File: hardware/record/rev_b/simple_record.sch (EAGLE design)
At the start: 24 parts, among them J1 SQUALL_HEADER, J2 PJ-102AH, J3 SCREW-TERMINAL_2_0.100, J4 SCREW-TERMINAL_2_0.100, Q1 MOSFET-NCHANNELSMD

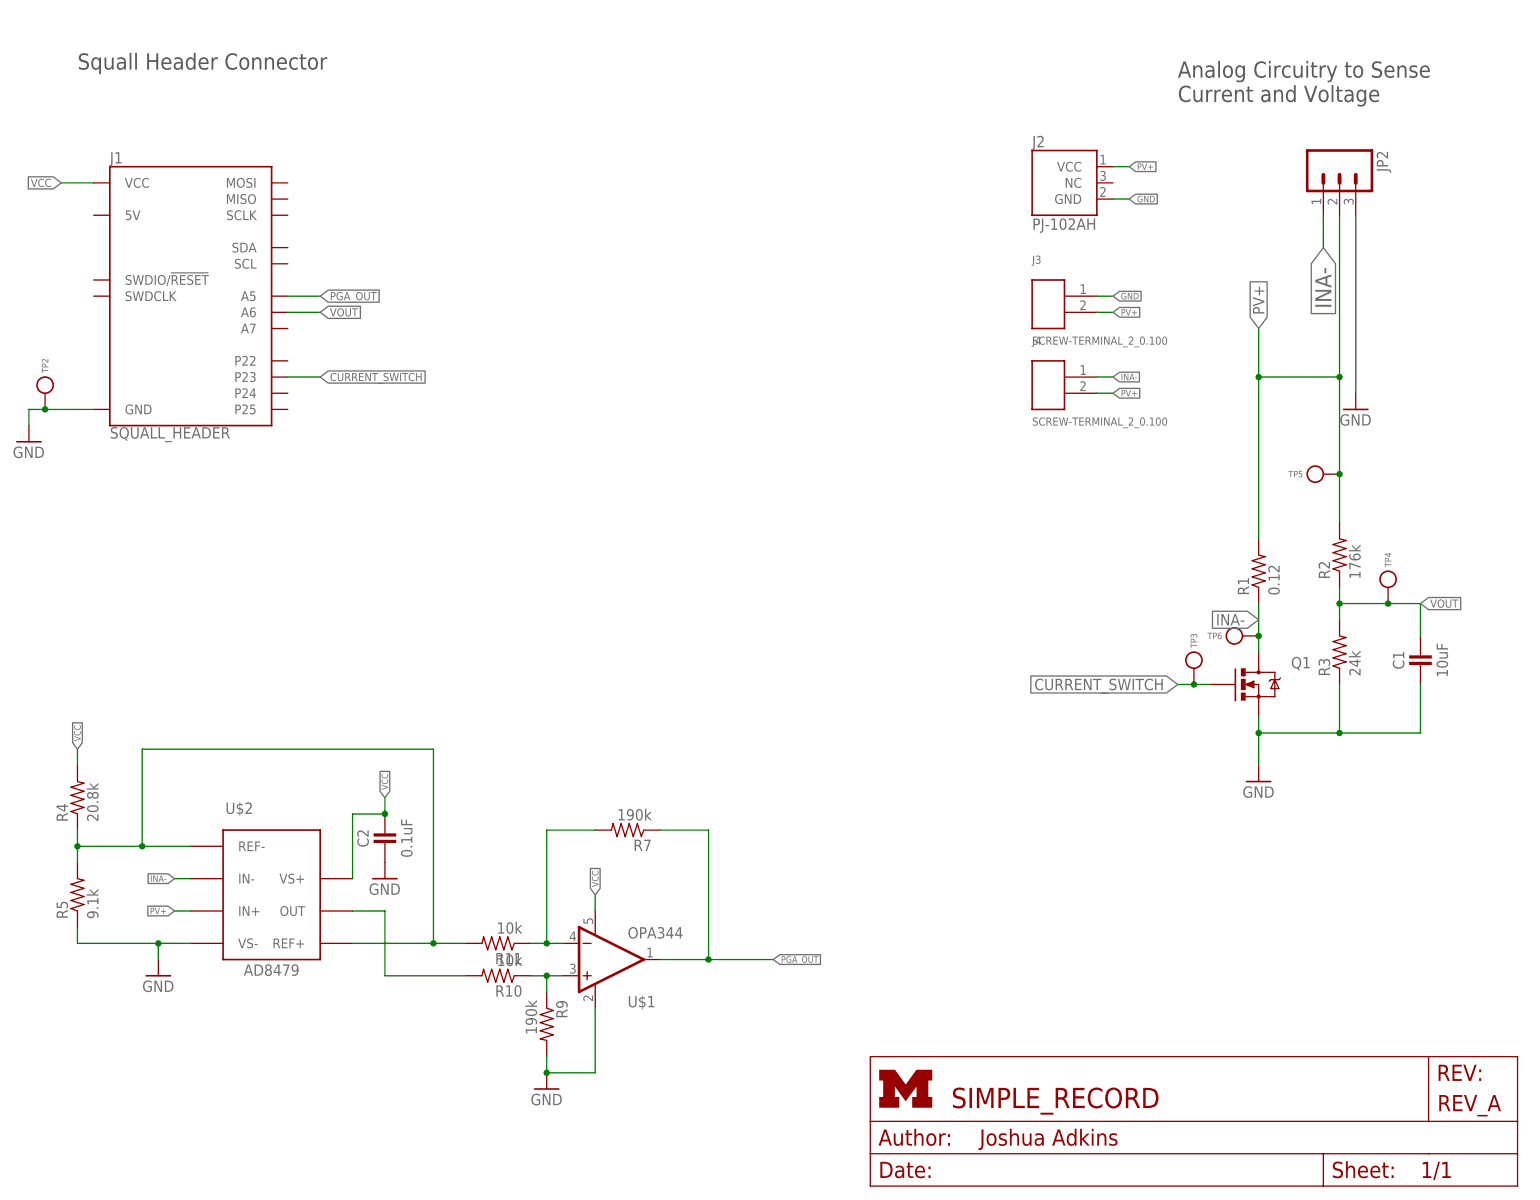
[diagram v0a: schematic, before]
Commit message: updated rev_b of the board to new chip
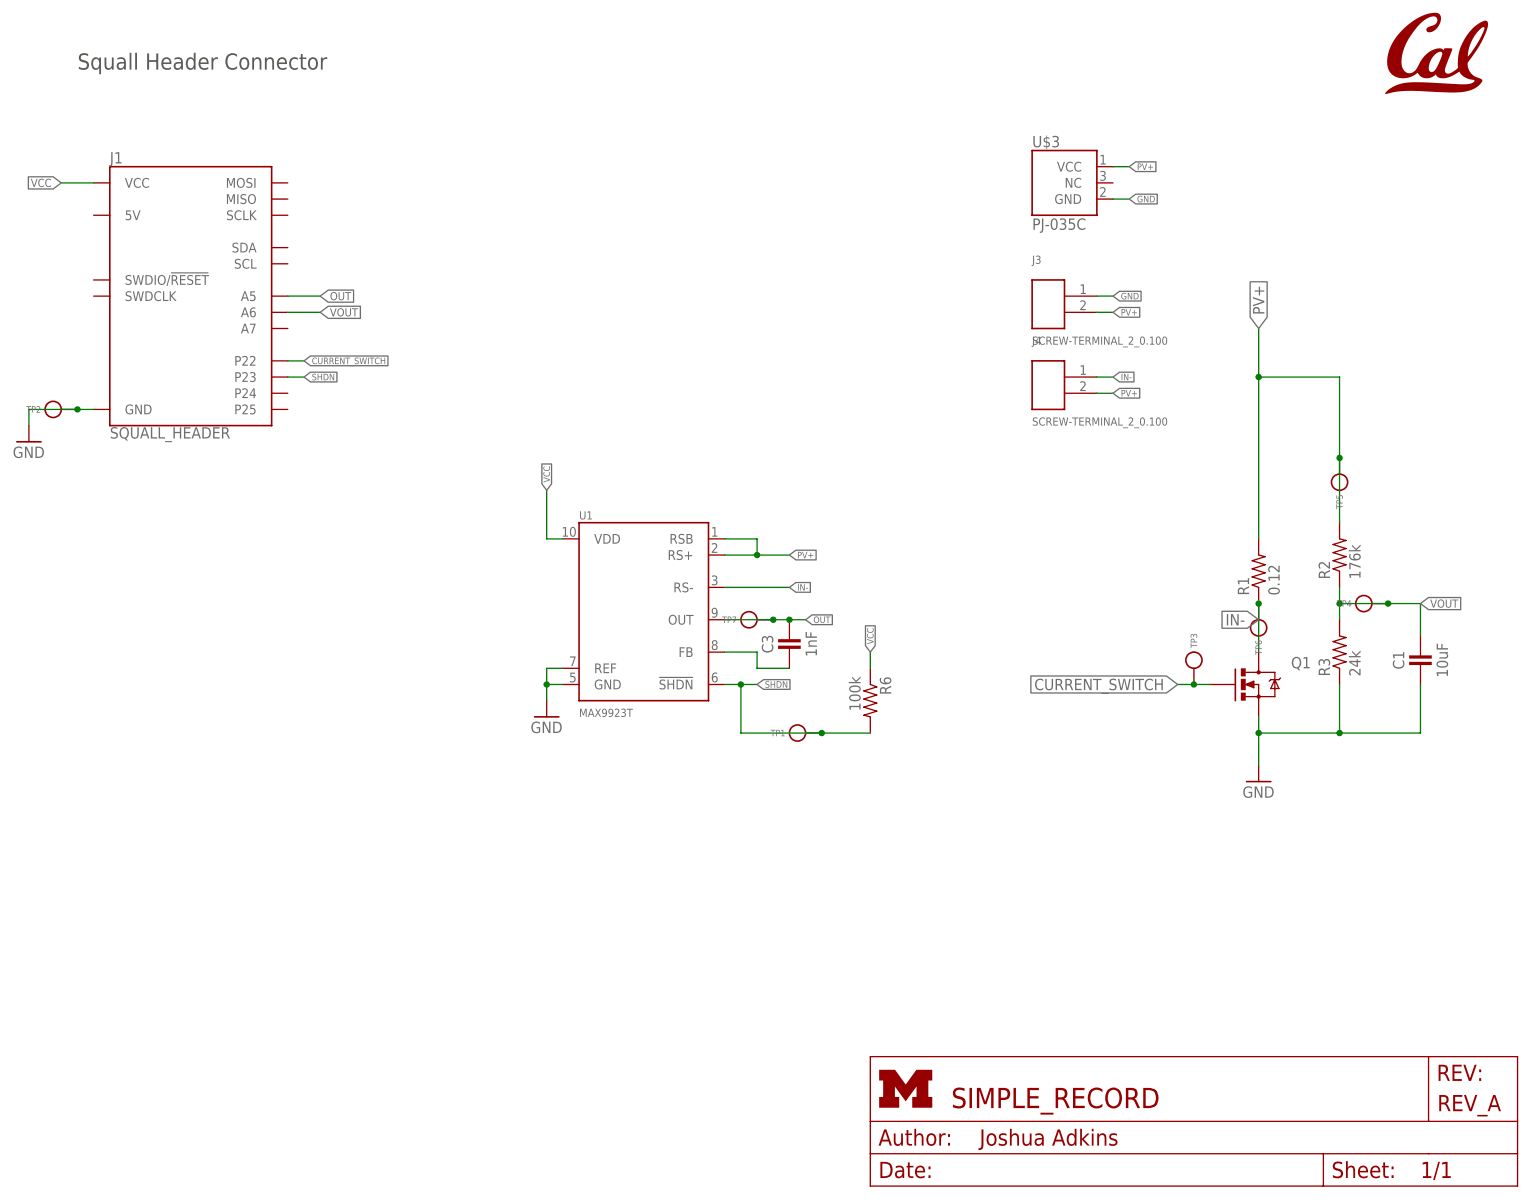
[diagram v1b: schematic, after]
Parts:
- removed C2: 0.1uF, passives:CAPACITOR
- removed J2: PJ-102AH, connector:PJ-102AH
- removed JP2: (no value), SparkFun-Connectors:M03PTH
- removed R10, R11: 10k, passives:RESISTOR
- removed R4: 20.8k, passives:RESISTOR
- removed R5: 9.1k, passives:RESISTOR
- removed R7, R9: 190k, passives:RESISTOR
- removed U$2: AD8479, chips:AD8479
- added C3: 1nF, passives:CAPACITOR
- added R6: 100k, passives:RESISTOR
- added TP1, TP7: TEST_POINT_0.040IN, headers:TEST_POINT_0.040IN
- added U$3: PJ-035C, connector:PJ-035C
- added U1: MAX9923T, chips:MAX9923H
- C1: device passives:CAPACITOR -> passives:CAPACITOR0603_CAP
- U$1: value OPA344 -> UCB_CAL75MIL; device SparkFun-AnalogIC:OPA344 -> logos:UCB_CAL75MIL
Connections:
- removed net INA-: J4.1, JP2.1, Q1.D, R1.1, TP6.TESTPOINT, U$2.IN-
- removed net N$2: R11.1, R7.2, U$1.-IN
- removed net N$3: R11.2, R4.1, R5.2, U$2.REF+, U$2.REF-
- removed net N$4: R10.1, R9.1, U$1.+IN
- removed net N$5: R10.2, U$2.OUT
- removed net PGA_OUT: J1.A5, R7.1, U$1.OUT
- new net IN-: J4.1, Q1.D, R1.1, TP6.TESTPOINT, U1.RS-
- new net N$7: C3.2, U1.FB
- new net OUT: C3.1, J1.A5, TP7.TESTPOINT, U1.OUT
- new net SHDN: J1.P23, R6.2, TP1.TESTPOINT, U1.!SHDN
- net CURRENT_SWITCH: now also J1.P22; no longer J1.P23
- net GND: now also U$3.GND, U1.GND, U1.REF; no longer C2.2, J2.GND, JP2.3, R5.1, R9.2, U$1.V-, U$2.VS-
- net PV+: now also U$3.VCC, U1.RS+, U1.RSB; no longer J2.VCC, JP2.2, U$2.IN+
- net VCC: now also R6.1, U1.VDD; no longer C2.1, R4.2, U$1.V+, U$2.VS+
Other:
- note removed: "Analog Circuitry to Sense Current and Voltage"
- moved on the sheet: TP2, TP4, TP5, TP6

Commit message: renumbered parts
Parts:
- removed C3: 1nF, passives:CAPACITOR
- removed R6: 100k, passives:RESISTOR
- added C2: 1nF, passives:CAPACITOR
- added R4: 176k, passives:RESISTOR
- R2: value 176k -> 24k
- R3: value 24k -> 100k
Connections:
- net GND: now also C2.2, R2.1; no longer C1.2, R3.1
- net N$7: now also C1.2; no longer C3.2
- net OUT: now also C1.1; no longer C3.1
- net PV+: now also R4.2; no longer R2.2
- net SHDN: now also R3.2; no longer R6.2
- net VCC: now also R3.1; no longer R6.1
- net VOUT: now also C2.1, R2.2, R4.1; no longer C1.1, R2.1, R3.2
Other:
- moved on the sheet: C1, R2, R3

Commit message: Revert "renumbered parts"
This reverts commit aba0891c6fa3a8957b5f6f1ce6d6696c13dad33f.

Something wonky happened there. I sure hope that commit message is
accurate and nothing else was changed...
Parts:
- removed C2: 1nF, passives:CAPACITOR
- removed R4: 176k, passives:RESISTOR
- added C3: 1nF, passives:CAPACITOR
- added R6: 100k, passives:RESISTOR
- R2: value 24k -> 176k
- R3: value 100k -> 24k
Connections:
- net GND: now also C1.2, R3.1; no longer C2.2, R2.1
- net N$7: now also C3.2; no longer C1.2
- net OUT: now also C3.1; no longer C1.1
- net PV+: now also R2.2; no longer R4.2
- net SHDN: now also R6.2; no longer R3.2
- net VCC: now also R6.1; no longer R3.1
- net VOUT: now also C1.1, R2.1, R3.2; no longer C2.1, R2.2, R4.1
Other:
- moved on the sheet: C1, R2, R3

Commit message: properly renumber parts
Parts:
- removed C3: 1nF, passives:CAPACITOR
- removed R6: 100k, passives:RESISTOR
- removed U$3: PJ-035C, connector:PJ-035C
- added C2: 10uF, passives:CAPACITOR0603_CAP
- added J2: SCREW-TERMINAL_2_0.100, headers:SCREW-TERMINAL_2_0.100
- added R4: 176k, passives:RESISTOR
- C1: value 10uF -> 1nF; device passives:CAPACITOR0603_CAP -> passives:CAPACITOR
- J1: value SQUALL_HEADER -> PJ-035C; device squall:SQUALL_HEADER -> connector:PJ-035C
- J4: value SCREW-TERMINAL_2_0.100 -> SQUALL_HEADER; device headers:SCREW-TERMINAL_2_0.100 -> squall:SQUALL_HEADER
- R2: value 176k -> 24k
- R3: value 24k -> 100k
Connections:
- net CURRENT_SWITCH: now also J4.P22; no longer J1.P22
- net GND: now also C2.2, J2.1, J4.GND, R2.1; no longer C1.2, J3.1, R3.1, U$3.GND
- net IN-: now also J3.1; no longer J4.1
- net N$7: now also C1.2; no longer C3.2
- net OUT: now also C1.1, J4.A5; no longer C3.1, J1.A5
- net PV+: now also J1.VCC, J2.2, R4.2; no longer J4.2, R2.2, U$3.VCC
- net SHDN: now also J4.P23, R3.2; no longer J1.P23, R6.2
- net VCC: now also J4.VCC, R3.1; no longer J1.VCC, R6.1
- net VOUT: now also C2.1, J4.A6, R2.2, R4.1; no longer C1.1, J1.A6, R2.1, R3.2
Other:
- moved on the sheet: C1, J3, R2, R3

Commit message: beautify
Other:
- moved on the sheet: C2, R1, R2, TP1, TP2, TP4, TP5, TP6, TP7

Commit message: updated board and bom
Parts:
- Q1: DIGIKEY (none) -> DMN3023L-7DICT-ND
- U1: DIGIKEY (none) -> MAX9923TEUB+TCT-ND
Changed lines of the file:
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@@
 <parts>
 <part name="FRAME1" library="frames" deviceset="LETTER_L" device=""/>
-<part name="Q1" library="fets" deviceset="MOSFET-NCHANNEL" device="SMD"/>
+<part name="Q1" library="fets" deviceset="MOSFET-NCHANNEL" device="SMD">
+<attribute name="DIGIKEY" value="DMN3023L-7DICT-ND"/>
+</part>
 <part name="GND2" library="SparkFun-Aesthetics" deviceset="GND" device=""/>
 <part name="R4" library="passives" deviceset="RESISTOR" device="" value="176k"/>
@@
 <part name="J3" library="headers" deviceset="SCREW-TERMINAL_2_0.100" device=""/>
 <part name="J1" library="connector" deviceset="PJ-035C" device=""/>
-<part name="U1" library="chips" deviceset="MAX992" device="3H" value="MAX9923T"/>
+<part name="U1" library="chips" deviceset="MAX992" device="3H" value="MAX9923T">
+<attribute name="DIGIKEY" value="MAX9923TEUB+TCT-ND"/>
+</part>
 <part name="GND3" library="SparkFun-Aesthetics" deviceset="GND" device=""/>
 <part name="C1" library="passives" deviceset="CAPACITOR" device="" value="1nF"/>
@@
 <instance part="Q1" gate="G$1" x="208.28" y="78.74" smashed="yes">
 <attribute name="NAME" x="210.82" y="81.28" size="1.778" layer="95"/>
+<attribute name="DIGIKEY" x="208.28" y="78.74" size="1.27" layer="96" align="bottom-center" display="off"/>
 </instance>
 <instance part="GND2" gate="1" x="208.28" y="66.04"/>

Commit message: updates
- added second barrel jack
- resized to be same size as logger board
- compressed test points to be 0.1" header friendly
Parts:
- added H1, H2: MOUNT-PAD-ROUND3.0, holes:MOUNT-PAD-ROUND3.0
- added J5: PJ-102AH, connector:PJ-102AH
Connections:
- net GND: now also H1.MOUNT, H2.MOUNT, J5.GND
- net PV+: now also J5.VCC
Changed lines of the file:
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@@
 <part name="TP7" library="headers" deviceset="TEST_POINT_0.040IN" device=""/>
 <part name="U$1" library="logos" deviceset="UCB_CAL" device="75MIL"/>
+<part name="H1" library="holes" deviceset="MOUNT-PAD-ROUND" device="3.0"/>
+<part name="H2" library="holes" deviceset="MOUNT-PAD-ROUND" device="3.0"/>
+<part name="GND1" library="SparkFun-Aesthetics" deviceset="GND" device=""/>
+<part name="J5" library="connector" deviceset="PJ-102AH" device=""/>
+<part name="GND5" library="SparkFun-Aesthetics" deviceset="GND" device=""/>
+<part name="GND6" library="SparkFun-Aesthetics" deviceset="GND" device=""/>
 </parts>
 <sheets>
@@
 <instance part="TP7" gate="G$1" x="129.54" y="91.44" rot="R270"/>
 <instance part="U$1" gate="G$1" x="236.22" y="177.8"/>
+<instance part="H1" gate="G$1" x="25.4" y="22.86"/>
+<instance part="H2" gate="G$1" x="25.4" y="17.78"/>
+<instance part="GND1" gate="1" x="20.32" y="12.7"/>
+<instance part="J5" gate="G$1" x="203.2" y="157.48"/>
+<instance part="GND5" gate="1" x="213.36" y="149.86"/>
+<instance part="GND6" gate="1" x="187.96" y="149.86"/>
 </instances>
 <busses>
@@
 <segment>
 <wire x1="185.42" y1="154.94" x2="187.96" y2="154.94" width="0.1524" layer="91"/>
-<label x="187.96" y="154.94" size="1.27" layer="95" xref="yes"/>
+<wire x1="187.96" y1="154.94" x2="187.96" y2="152.4" width="0.1524" layer="91"/>
 <pinref part="J1" gate="G$1" pin="GND"/>
+<pinref part="GND6" gate="1" pin="GND"/>
 </segment>
 <segment>
@@
 <wire x1="96.52" y1="81.28" x2="96.52" y2="78.74" width="0.1524" layer="91"/>
 <junction x="96.52" y="78.74"/>
+</segment>
+<segment>
+<pinref part="H1" gate="G$1" pin="MOUNT"/>
+<wire x1="22.86" y1="22.86" x2="20.32" y2="22.86" width="0.1524" layer="91"/>
+<wire x1="20.32" y1="22.86" x2="20.32" y2="17.78" width="0.1524" layer="91"/>
+<pinref part="H2" gate="G$1" pin="MOUNT"/>
+<wire x1="20.32" y1="17.78" x2="22.86" y2="17.78" width="0.1524" layer="91"/>
+<wire x1="20.32" y1="17.78" x2="20.32" y2="15.24" width="0.1524" layer="91"/>
+<junction x="20.32" y="17.78"/>
+<pinref part="GND1" gate="1" pin="GND"/>
+</segment>
+<segment>
+<pinref part="J5" gate="G$1" pin="GND"/>
+<wire x1="210.82" y1="154.94" x2="213.36" y2="154.94" width="0.1524" layer="91"/>
+<pinref part="GND5" gate="1" pin="GND"/>
+<wire x1="213.36" y1="154.94" x2="213.36" y2="152.4" width="0.1524" layer="91"/>
 </segment>
 </net>
@@
 <label x="134.62" y="99.06" size="1.27" layer="95" xref="yes"/>
 </segment>
+<segment>
+<pinref part="J5" gate="G$1" pin="VCC"/>
+<wire x1="210.82" y1="160.02" x2="213.36" y2="160.02" width="0.1524" layer="91"/>
+<label x="213.36" y="160.02" size="1.27" layer="95" xref="yes"/>
+</segment>
 </net>
